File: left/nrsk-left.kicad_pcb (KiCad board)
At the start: 2 copper layers, 161.1 x 133.5 mm, 125 parts, among them J1 USB-C, J2 USB-C, J3 OLED 128x32, SW1 Esc, SW10 2, SW11 3, SW12 4, SW13 5, SW14 6, SW15 Tab, SW16 Q, SW17 W, SW18 E, SW19 R, SW2 F1, SW20 T, SW21 Ctrl, SW22 A, SW23 S, SW24 D, SW25 F, SW26 G, SW27 Shift, SW28 Z, SW29 X, SW3 F2, SW30 C, SW31 V, SW32 B, SW33 Ctrl, SW34 Opt, SW35 Cmd, SW36 Space, SW37 Space, SW38 Space, SW4 F3, SW5 F4, SW6 F5, SW7 F6, SW8 `, SW9 1, U1 RP2040, U2 USBLC6-2SC6, U4 AP2112K-3.3, U5 W25Q128JVS, Y1 12MHz

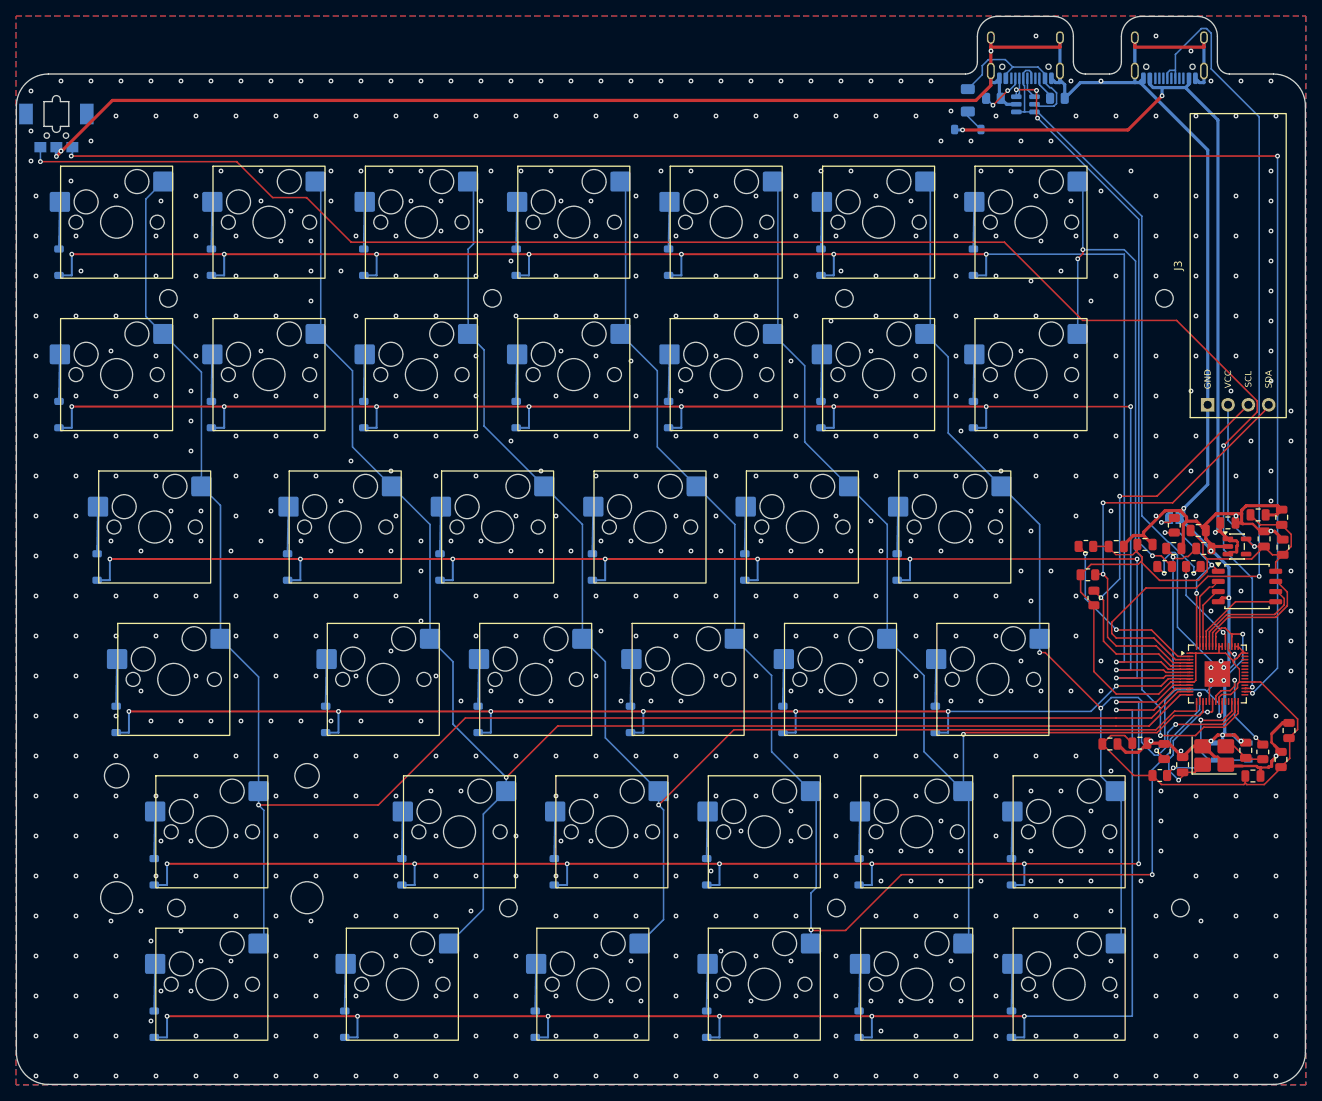
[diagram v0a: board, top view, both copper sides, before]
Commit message: Back to single-sided assembly; RP2040 window with a clear acrylic lid in the case floor
- PCB: the RP2040 and its support parts go back to the back side (reverts the placement of
  a6faa8b): every assembled part is on the back again, so JLC assembles one side.
  make_jlc refuses top-side parts again; the front assembly drawing is gone. Kept from
  a6faa8b: the routing retry until 0 unconnected and 0 DRC violations, and the USB-C
  footprint with its outline on Fab
- make_pcb writes the RP2040 and flash courtyards to case_data.json (mcu)
- Case: a rounded window in the tray floor / acrylic bottom plate, 2 mm round the RP2040
  and flash, R2. Clear 1.5 mm acrylic lid (case/laser/<side>-mcu-lid), 3 mm past the window
  (at least 2 mm where the wall is close, there cut back to the wall), taped on the inner
  face of the floor; the printed tray has a 1.8 mm rim round it. Checks: window shows both
  parts, lid clear of the wall, standoffs, reset hole and wheel, 3 mm of floor to the reset
  hole (laser shop's minimum)
- Printed plate B: no cut-outs for front parts any more
- BOM (lid, tape), ordering / checklist (Bottom-side assembly, lid DXF), assembly guide
  (lid step before the board), viewer and Blender scene (lid; board loaded in B as well,
  for the view through the window), README
- Checked: DRC 0 / unconnected 0 / parity 0 / ERC 0 on both halves; JLC CPL all Bottom
  (77 left, 81 right); make_case checks ok; textlint 0 on README, ordering, checklist

Co-Authored-By: Claude Opus 5.5 <noreply@anthropic.com>
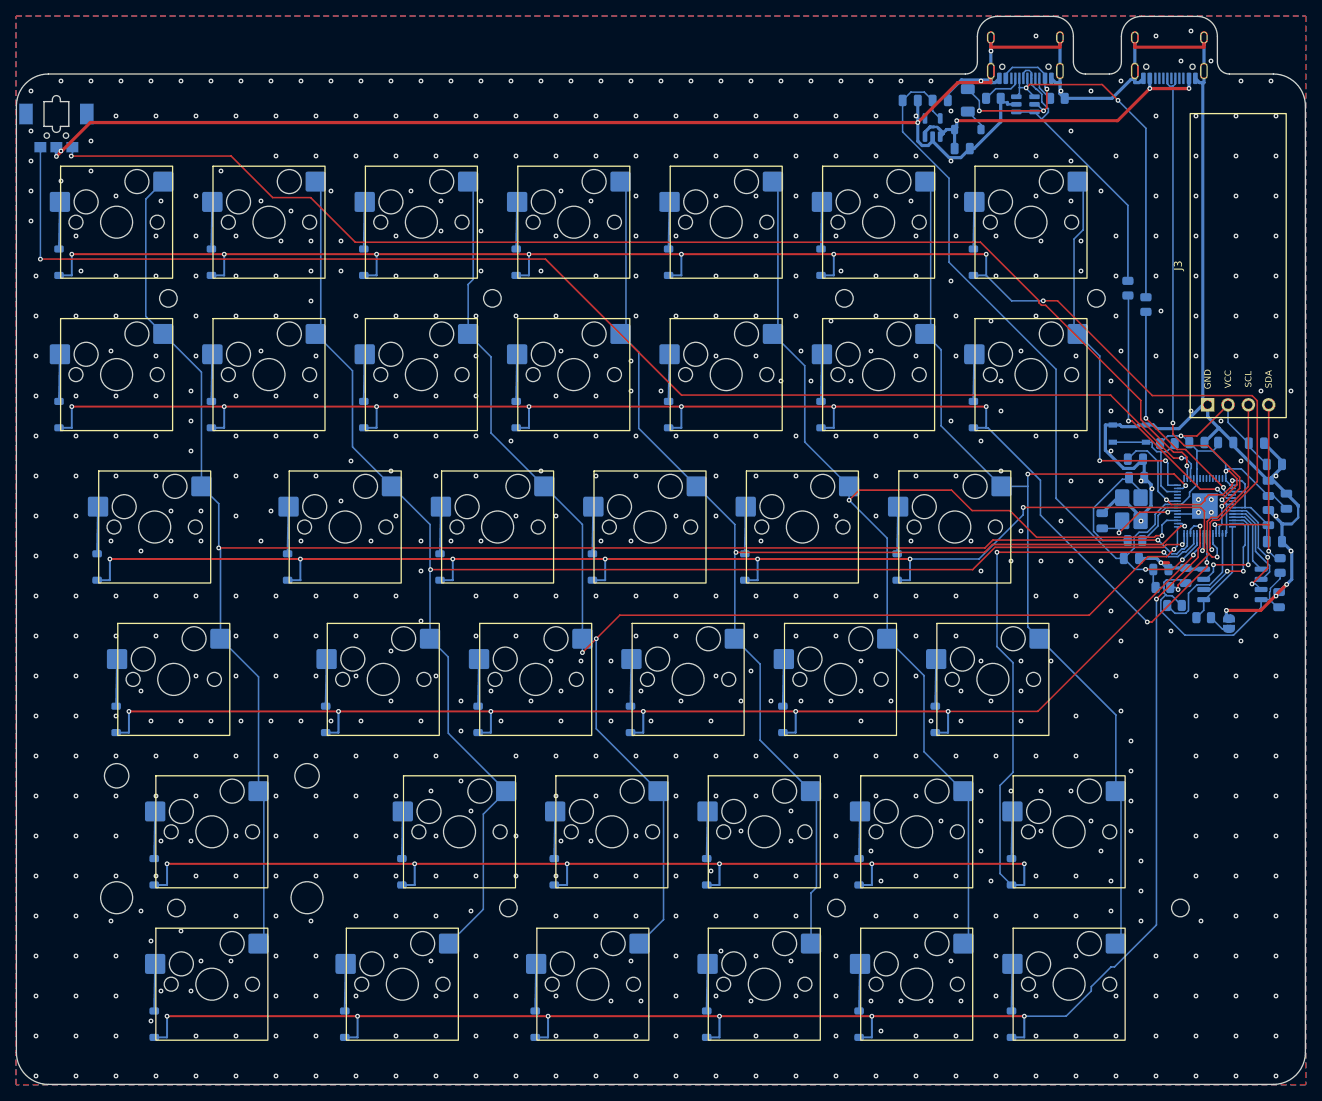
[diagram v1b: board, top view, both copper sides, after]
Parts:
- C1, C11, C12, C13, C14, C15, C16, C17, C18, C19, C2, C20, C3, C4, C5, C6, C7, C8, R1, R10, R2, R3, R6, R7, R8, R9, U1, U4, U5, Y1: moved to B.Cu
- moved C17 68.1 mm to (142.5, 24.3), turned to 0 degrees
- moved C19 67.6 mm to (138.7, 24.3)
- moved U4 64.7 mm to (141.5, 27.7), turned to 90 degrees
- moved C16 57.4 mm to (145.2, 30.3)
- moved C12 42.3 mm to (174.6, 67.1)
- moved RSW1 41.7 mm to (166.1, 66.0)
- moved R6 41.5 mm to (170.9, 67.2)
- moved C2 36.7 mm to (167.0, 71.5), turned to 0 degrees
- moved C5 36.7 mm to (166.9, 69.2), turned to 0 degrees
- moved R2 35.7 mm to (165.9, 47.8), turned to 90 degrees
- moved R3 32.8 mm to (168.2, 49.8), turned to 90 degrees
- moved Y1 32.5 mm to (166.4, 75.4), turned to 90 degrees
- moved C1 32.1 mm to (162.7, 76.8)
- moved C11 31.3 mm to (166.4, 81.5), turned to 0 degrees
- moved R10 30.9 mm to (166.8, 79.3), turned to 0 degrees
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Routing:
- net /ENC_A: track 221.4 -> 160.5 mm, vias 3 -> 2
- net VCC: track 99.9 -> 42.5 mm
- net /COL6: track 99.7 -> 49.6 mm, vias 3 -> 2
- net /DATA: track 114.6 -> 64.8 mm, vias 1 -> 2
- net /USB_D+: track 76.6 -> 37.3 mm, vias 1 -> 0
- net /ENC_B: track 206.4 -> 170.3 mm, vias 3 -> 2
- net /USB_D-: track 76.6 -> 44.7 mm, vias 4 -> 2
- net /SDA: track 55.6 -> 28.0 mm
- net /3V3: track 171.8 -> 197.3 mm, vias 1 -> 5
- net /ROW4: track 180.1 -> 203.1 mm
- net /1V1: track 57.9 -> 35.5 mm, vias 4 -> 2
- net /D+: track 12.0 -> 32.7 mm
- net /SCL: track 53.4 -> 32.8 mm
- net /ROW1: track 206.2 -> 191.3 mm
- net /ROW0: track 222.9 -> 208.2 mm, vias 8 -> 9
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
